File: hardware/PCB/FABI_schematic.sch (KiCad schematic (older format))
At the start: 46 parts, among them J1 Cliff_68125, J10 Conn_01x03_Male, J11 dispaly_connector_91601-304LF, J2 Cliff_68125, J3 Cliff_68125, J4 Cliff_68125, J5 Cliff_68125, J6 Cliff_68125, J7 Cliff_68125, J8 Cliff_68125, J9 Conn_02x05_Odd_Even, U1 MPXV7007GP, U2 ProMicro

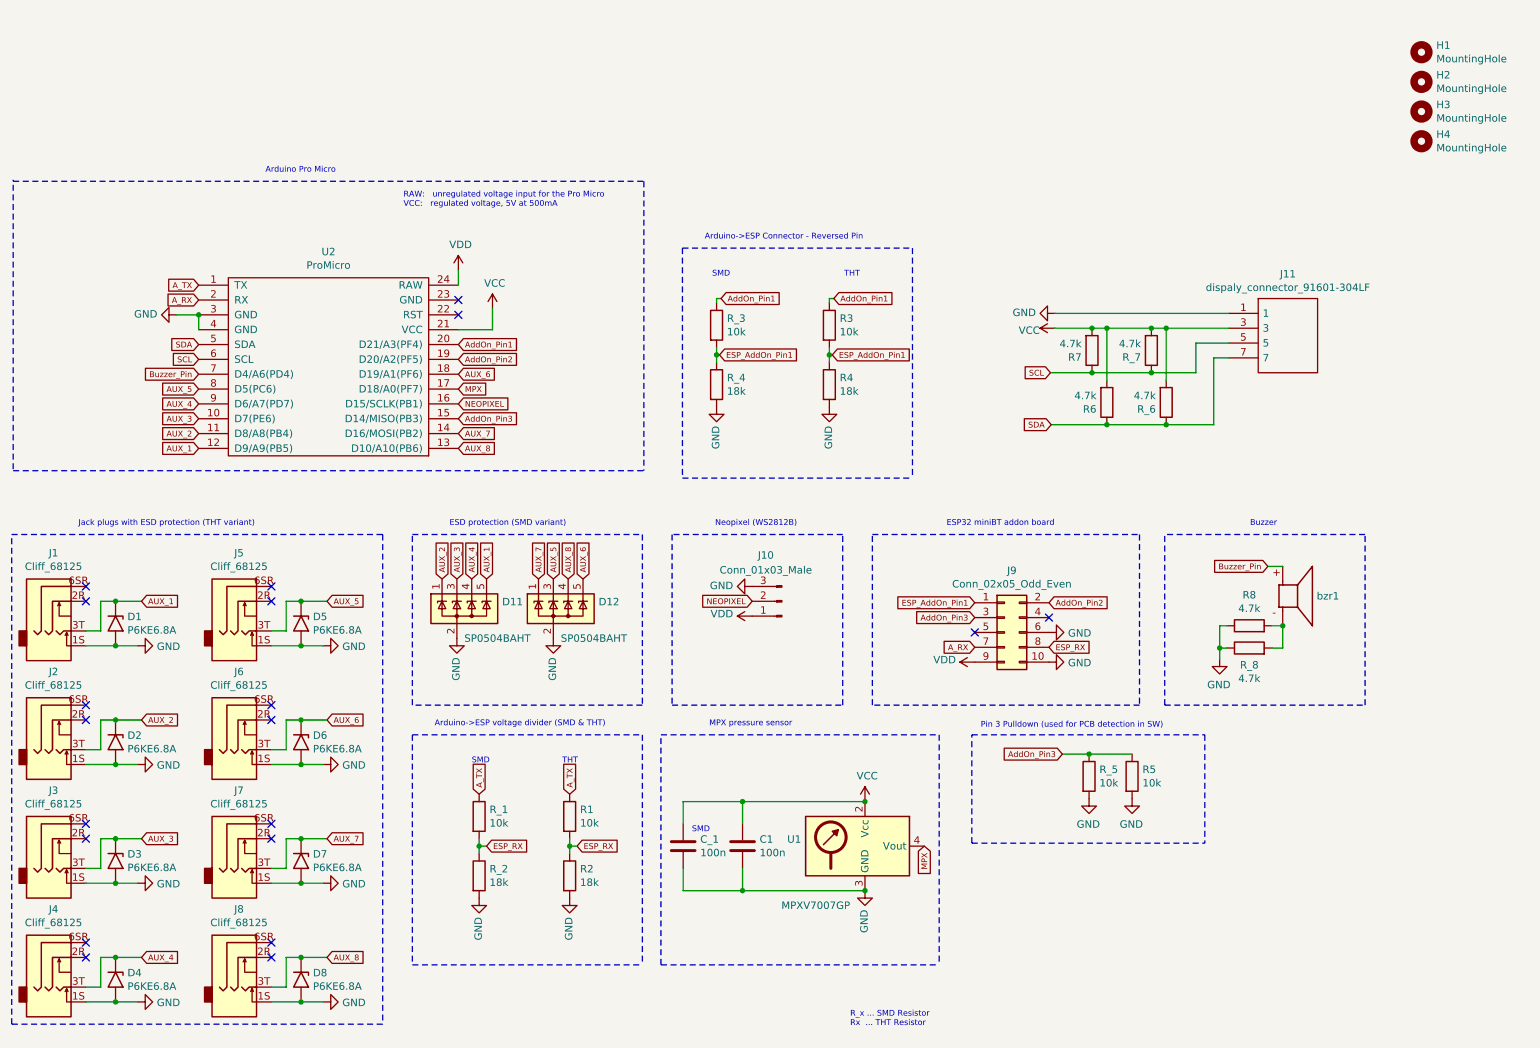
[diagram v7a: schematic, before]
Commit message: updated PCB edges, to mount PCB with M3 screws, minor changes to size and some element positions, SMD NeoPixel pads updated
Signed-off-by: fussthalerandreas <fussthaler.andreas1997@gmail.com>
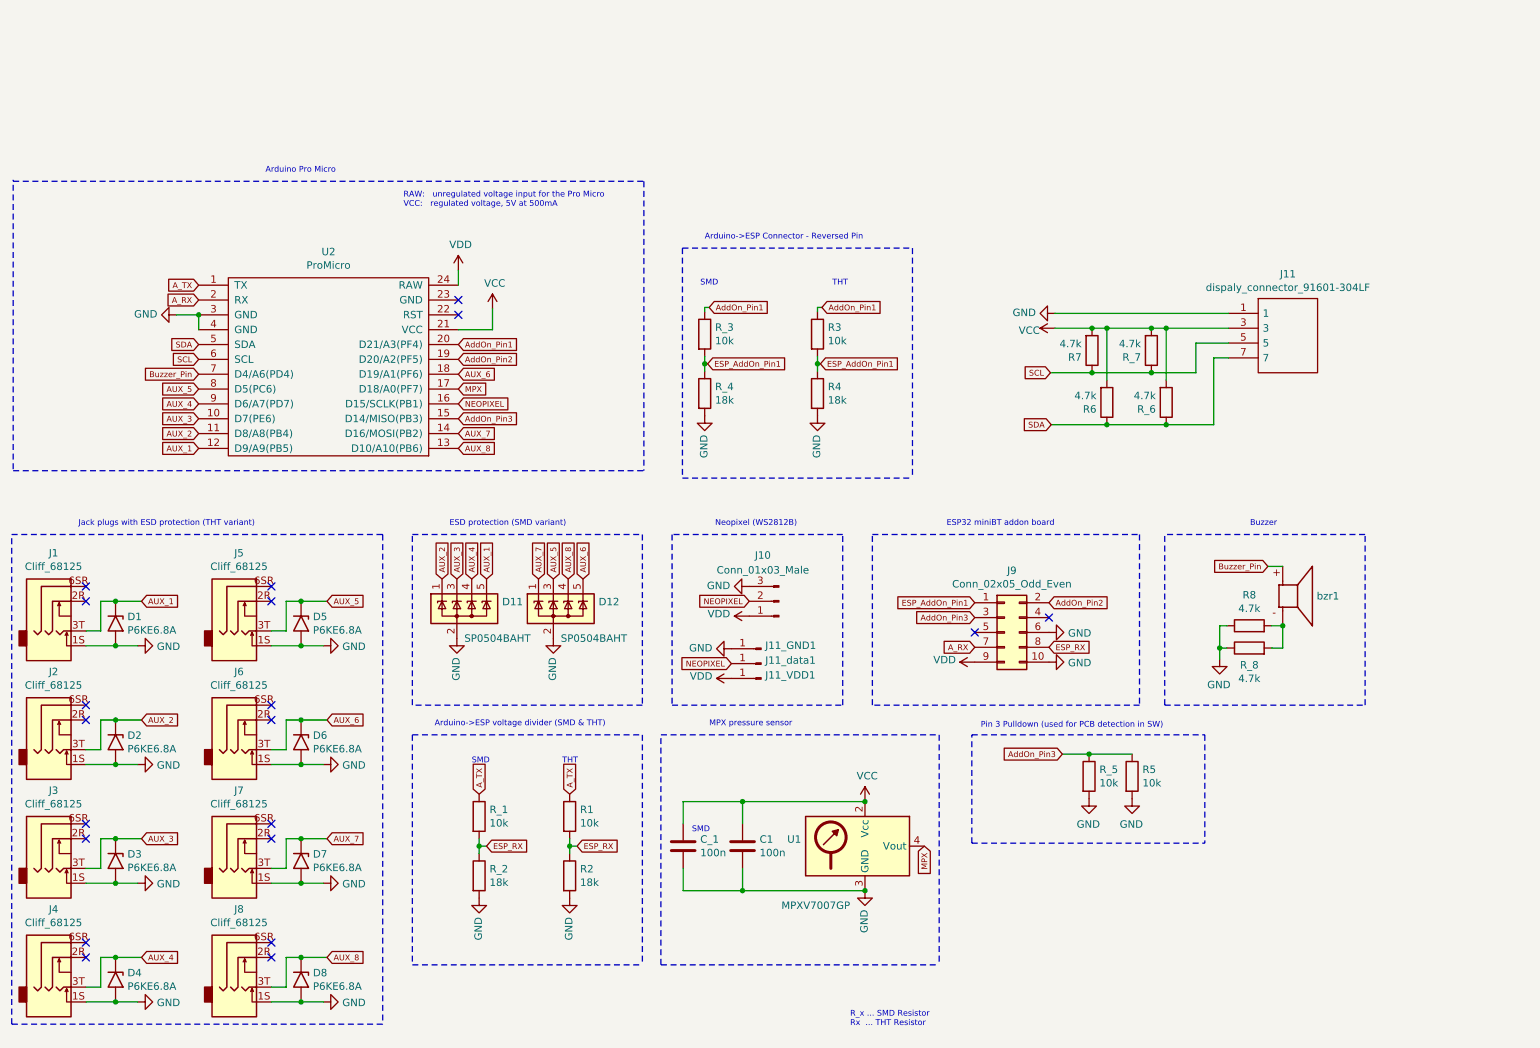
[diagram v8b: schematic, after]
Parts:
- removed H1, H2, H3, H4: MountingHole, MountingHole:MountingHole_3mm, symbol Mechanical:MountingHole
- added J11_GND1, J11_VDD1, J11_data1: Conn_01x01_Male, Connector_Wire:SolderWirePad_1x01_SMD_1x2mm, symbol Connector:Conn_01x01_Male
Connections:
- net GND: now also J11_GND1.1 (Pin_1)
- net NEOPIXEL: now also J11_data1.1 (Pin_1)
- net VDD: now also J11_VDD1.1 (Pin_1)
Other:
- moved on the sheet: J10, R3, R4, R_3, R_4
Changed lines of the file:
@@
 NoConn ~ 7590 4910
 NoConn ~ 7090 5010
-$Comp
-L Device:R R4
-U 1 1 6021AB8E
-P 6110 3340
-F 0 "R4" H 6180 3386 50  0000 L CNN
-F 1 "18k" H 6180 3295 50  0000 L CNN
-F 2 "Resistor_THT:R_Axial_DIN0204_L3.6mm_D1.6mm_P7.62mm_Horizontal" V 6040 3340 50  0001 C CNN
-F 3 "~" H 6110 3340 50  0001 C CNN
-	1    6110 3340
-	1    0    0    -1
-$EndComp
-$Comp
-L Device:R R3
-U 1 1 6021AB94
-P 6110 2940
-F 0 "R3" H 6180 2986 50  0000 L CNN
-F 1 "10k" H 6180 2895 50  0000 L CNN
-F 2 "Resistor_THT:R_Axial_DIN0204_L3.6mm_D1.6mm_P7.62mm_Horizontal" V 6040 2940 50  0001 C CNN
-F 3 "~" H 6110 2940 50  0001 C CNN
-	1    6110 2940
-	1    0    0    -1
-$EndComp
-Wire Wire Line
-	6110 3090 6110 3140
-$Comp
-L power:GND #PWR022
-U 1 1 6021AB9D
-P 6110 3490
-F 0 "#PWR022" H 6110 3240 50  0001 C CNN
-F 1 "GND" V 6115 3362 50  0000 R CNN
-F 2 "" H 6110 3490 50  0001 C CNN
-F 3 "" H 6110 3490 50  0001 C CNN
-	1    6110 3490
-	-1   0    0    -1
-$EndComp
-$Comp
-L Device:R R_4
-U 1 1 6021ABA3
-P 5350 3340
-F 0 "R_4" H 5420 3386 50  0000 L CNN
-F 1 "18k" H 5420 3295 50  0000 L CNN
-F 2 "Resistor_SMD:R_0805_2012Metric_Pad1.20x1.40mm_HandSolder" V 5280 3340 50  0001 C CNN
-F 3 "~" H 5350 3340 50  0001 C CNN
-	1    5350 3340
-	1    0    0    -1
-$EndComp
-$Comp
-L Device:R R_3
-U 1 1 6021ABA9
-P 5350 2940
-F 0 "R_3" H 5420 2986 50  0000 L CNN
-F 1 "10k" H 5420 2895 50  0000 L CNN
-F 2 "Resistor_SMD:R_0805_2012Metric_Pad1.20x1.40mm_HandSolder" V 5280 2940 50  0001 C CNN
-F 3 "~" H 5350 2940 50  0001 C CNN
-	1    5350 2940
-	1    0    0    -1
-$EndComp
-Wire Wire Line
-	5350 3090 5350 3140
-$Comp
-L power:GND #PWR021
-U 1 1 6021ABB2
-P 5350 3490
-F 0 "#PWR021" H 5350 3240 50  0001 C CNN
-F 1 "GND" V 5355 3362 50  0000 R CNN
-F 2 "" H 5350 3490 50  0001 C CNN
-F 3 "" H 5350 3490 50  0001 C CNN
-	1    5350 3490
-	-1   0    0    -1
-$EndComp
-Text Notes 6210 2620 0    39   ~ 0
+Text Notes 6130 2680 0    39   ~ 0
 THT
-Text Notes 5320 2620 0    39   ~ 0
+Text Notes 5240 2680 0    39   ~ 0
 SMD
 Wire Notes Line
@@
 	6670 2420 6670 3970
 Wire Wire Line
-	5380 2760 5350 2760
-Wire Wire Line
-	5350 2760 5350 2790
-Wire Wire Line
-	6140 2760 6110 2760
-Wire Wire Line
-	6110 2760 6110 2790
-Text GLabel 5370 3140 2    39   Input ~ 0
-ESP_AddOn_Pin1
-Text GLabel 6130 3140 2    39   Input ~ 0
-ESP_AddOn_Pin1
-Wire Wire Line
-	6130 3140 6110 3140
-Connection ~ 6110 3140
-Wire Wire Line
-	6110 3140 6110 3190
-Wire Wire Line
-	5370 3140 5350 3140
-Connection ~ 5350 3140
-Wire Wire Line
-	5350 3140 5350 3190
+	5300 2820 5270 2820
+Wire Wire Line
+	5270 2820 5270 2850
+Wire Wire Line
+	6060 2820 6030 2820
+Wire Wire Line
+	6030 2820 6030 2850
 Wire Wire Line
 	3610 2970 3840 2970
@@
 Text GLabel 3610 3470 2    39   Input ~ 0
 NEOPIXEL
-Text GLabel 5590 4800 0    39   Input ~ 0
+Text GLabel 5570 4800 0    39   Input ~ 0
 NEOPIXEL
 $Comp
 L power:GND #PWR016
 U 1 1 5F4DD6BE
-P 5590 4700
-F 0 "#PWR016" H 5590 4450 50  0001 C CNN
-F 1 "GND" V 5595 4572 50  0000 R CNN
-F 2 "" H 5590 4700 50  0001 C CNN
-F 3 "" H 5590 4700 50  0001 C CNN
-	1    5590 4700
+P 5570 4700
+F 0 "#PWR016" H 5570 4450 50  0001 C CNN
+F 1 "GND" V 5575 4572 50  0000 R CNN
+F 2 "" H 5570 4700 50  0001 C CNN
+F 3 "" H 5570 4700 50  0001 C CNN
+	1    5570 4700
 	0    1    -1   0
 $EndComp
@@
 L Connector:Conn_01x03_Male J10
 U 1 1 5F4DCE7D
-P 5790 4800
-F 0 "J10" H 5898 4490 50  0000 C CNN
-F 1 "Conn_01x03_Male" H 5898 4590 50  0000 C CNN
-F 2 "Connector_PinHeader_2.54mm:PinHeader_1x03_P2.54mm_Vertical" H 5790 4800 50  0001 C CNN
-F 3 "~" H 5790 4800 50  0001 C CNN
-	1    5790 4800
+P 5770 4800
+F 0 "J10" H 5878 4490 50  0000 C CNN
+F 1 "Conn_01x03_Male" H 5878 4590 50  0000 C CNN
+F 2 "Connector_PinHeader_2.54mm:PinHeader_1x03_P2.54mm_Vertical" H 5770 4800 50  0001 C CNN
+F 3 "~" H 5770 4800 50  0001 C CNN
+	1    5770 4800
 	-1   0    0    1
 $EndComp
@@
 L power:VDD #PWR0103
 U 1 1 6031B043
-P 5590 4900
-F 0 "#PWR0103" H 5590 4750 50  0001 C CNN
-F 1 "VDD" V 5605 5028 50  0000 L CNN
-F 2 "" H 5590 4900 50  0001 C CNN
-F 3 "" H 5590 4900 50  0001 C CNN
-	1    5590 4900
+P 5570 4900
+F 0 "#PWR0103" H 5570 4750 50  0001 C CNN
+F 1 "VDD" V 5585 5028 50  0000 L CNN
+F 2 "" H 5570 4900 50  0001 C CNN
+F 3 "" H 5570 4900 50  0001 C CNN
+	1    5570 4900
 	0    -1   -1   0
 $EndComp
 Wire Wire Line
 	8380 2960 8800 2960
-Text GLabel 6140 2760 2    39   Input ~ 0
+Text GLabel 6060 2820 2    39   Input ~ 0
 AddOn_Pin1
-Text GLabel 5380 2760 2    39   Input ~ 0
+Text GLabel 5300 2820 2    39   Input ~ 0
 AddOn_Pin1
 Text GLabel 3610 3570 2    39   Input ~ 0
@@
 Text GLabel 3610 3770 2    39   Input ~ 0
 AUX_8
-$Comp
-L Mechanical:MountingHole H1
-U 1 1 606D8EE1
-P 10100 1100
-F 0 "H1" H 10200 1146 50  0000 L CNN
-F 1 "MountingHole" H 10200 1055 50  0000 L CNN
-F 2 "MountingHole:MountingHole_3mm" H 10100 1100 50  0001 C CNN
-F 3 "~" H 10100 1100 50  0001 C CNN
-	1    10100 1100
-	1    0    0    -1
-$EndComp
-$Comp
-L Mechanical:MountingHole H2
-U 1 1 606D952C
-P 10100 1300
-F 0 "H2" H 10200 1346 50  0000 L CNN
-F 1 "MountingHole" H 10200 1255 50  0000 L CNN
-F 2 "MountingHole:MountingHole_3mm" H 10100 1300 50  0001 C CNN
-F 3 "~" H 10100 1300 50  0001 C CNN
-	1    10100 1300
-	1    0    0    -1
-$EndComp
-$Comp
-L Mechanical:MountingHole H3
-U 1 1 606DCA97
-P 10100 1500
-F 0 "H3" H 10200 1546 50  0000 L CNN
-F 1 "MountingHole" H 10200 1455 50  0000 L CNN
-F 2 "MountingHole:MountingHole_3mm" H 10100 1500 50  0001 C CNN
-F 3 "~" H 10100 1500 50  0001 C CNN
-	1    10100 1500
-	1    0    0    -1
-$EndComp
-$Comp
-L Mechanical:MountingHole H4
-U 1 1 606DFEF8
-P 10100 1700
-F 0 "H4" H 10200 1746 50  0000 L CNN
-F 1 "MountingHole" H 10200 1655 50  0000 L CNN
-F 2 "MountingHole:MountingHole_3mm" H 10100 1700 50  0001 C CNN
-F 3 "~" H 10100 1700 50  0001 C CNN
-	1    10100 1700
-	1    0    0    -1
-$EndComp
 Wire Notes Line
 	4975 5700 6850 5700
@@
 	1    0    0    1
 $EndComp
+Text GLabel 5450 5220 0    39   Input ~ 0
+NEOPIXEL
+$Comp
+L power:GND #PWR015
+U 1 1 60329107
+P 5450 5120
+F 0 "#PWR015" H 5450 4870 50  0001 C CNN
+F 1 "GND" V 5455 4992 50  0000 R CNN
+F 2 "" H 5450 5120 50  0001 C CNN
+F 3 "" H 5450 5120 50  0001 C CNN
+	1    5450 5120
+	0    1    -1   0
+$EndComp
+$Comp
+L power:VDD #PWR028
+U 1 1 6032910D
+P 5450 5320
+F 0 "#PWR028" H 5450 5170 50  0001 C CNN
+F 1 "VDD" V 5465 5448 50  0000 L CNN
+F 2 "" H 5450 5320 50  0001 C CNN
+F 3 "" H 5450 5320 50  0001 C CNN
+	1    5450 5320
+	0    -1   -1   0
+$EndComp
+$Comp
+L Connector:Conn_01x01_Male J11_data1
+U 1 1 6032D010
+P 5650 5220
+F 0 "J11_data1" H 5622 5198 50  0000 R CNN
+F 1 "Conn_01x01_Male" H 5622 5243 50  0001 R CNN
+F 2 "Connector_Wire:SolderWirePad_1x01_SMD_1x2mm" H 5650 5220 50  0001 C CNN
+F 3 "~" H 5650 5220 50  0001 C CNN
+	1    5650 5220
+	-1   0    0    1
+$EndComp
+$Comp
+L Connector:Conn_01x01_Male J11_GND1
+U 1 1 60327A50
+P 5650 5120
+F 0 "J11_GND1" H 5622 5098 50  0000 R CNN
+F 1 "Conn_01x01_Male" H 5622 5143 50  0001 R CNN
+F 2 "Connector_Wire:SolderWirePad_1x01_SMD_1x2mm" H 5650 5120 50  0001 C CNN
+F 3 "~" H 5650 5120 50  0001 C CNN
+	1    5650 5120
+	-1   0    0    1
+$EndComp
+$Comp
+L Connector:Conn_01x01_Male J11_VDD1
+U 1 1 603306CD
+P 5650 5320
+F 0 "J11_VDD1" H 5622 5298 50  0000 R CNN
+F 1 "Conn_01x01_Male" H 5622 5343 50  0001 R CNN
+F 2 "Connector_Wire:SolderWirePad_1x01_SMD_1x2mm" H 5650 5320 50  0001 C CNN
+F 3 "~" H 5650 5320 50  0001 C CNN
+	1    5650 5320
+	-1   0    0    1
+$EndComp
+Wire Wire Line
+	5270 3200 5270 3250
+Connection ~ 5270 3200
+Wire Wire Line
+	5290 3200 5270 3200
+Wire Wire Line
+	6030 3200 6030 3250
+Connection ~ 6030 3200
+Wire Wire Line
+	6050 3200 6030 3200
+Text GLabel 6050 3200 2    39   Input ~ 0
+ESP_AddOn_Pin1
+Text GLabel 5290 3200 2    39   Input ~ 0
+ESP_AddOn_Pin1
+$Comp
+L power:GND #PWR021
+U 1 1 6021ABB2
+P 5270 3550
+F 0 "#PWR021" H 5270 3300 50  0001 C CNN
+F 1 "GND" V 5275 3422 50  0000 R CNN
+F 2 "" H 5270 3550 50  0001 C CNN
+F 3 "" H 5270 3550 50  0001 C CNN
+	1    5270 3550
+	-1   0    0    -1
+$EndComp
+Wire Wire Line
+	5270 3150 5270 3200
+$Comp
+L Device:R R_3
+U 1 1 6021ABA9
+P 5270 3000
+F 0 "R_3" H 5340 3046 50  0000 L CNN
+F 1 "10k" H 5340 2955 50  0000 L CNN
+F 2 "Resistor_SMD:R_0805_2012Metric_Pad1.20x1.40mm_HandSolder" V 5200 3000 50  0001 C CNN
+F 3 "~" H 5270 3000 50  0001 C CNN
+	1    5270 3000
+	1    0    0    -1
+$EndComp
+$Comp
+L Device:R R_4
+U 1 1 6021ABA3
+P 5270 3400
+F 0 "R_4" H 5340 3446 50  0000 L CNN
+F 1 "18k" H 5340 3355 50  0000 L CNN
+F 2 "Resistor_SMD:R_0805_2012Metric_Pad1.20x1.40mm_HandSolder" V 5200 3400 50  0001 C CNN
+F 3 "~" H 5270 3400 50  0001 C CNN
+	1    5270 3400
+	1    0    0    -1
+$EndComp
+$Comp
+L power:GND #PWR022
+U 1 1 6021AB9D
+P 6030 3550
+F 0 "#PWR022" H 6030 3300 50  0001 C CNN
+F 1 "GND" V 6035 3422 50  0000 R CNN
+F 2 "" H 6030 3550 50  0001 C CNN
+F 3 "" H 6030 3550 50  0001 C CNN
+	1    6030 3550
+	-1   0    0    -1
+$EndComp
+Wire Wire Line
+	6030 3150 6030 3200
+$Comp
+L Device:R R3
+U 1 1 6021AB94
+P 6030 3000
+F 0 "R3" H 6100 3046 50  0000 L CNN
+F 1 "10k" H 6100 2955 50  0000 L CNN
+F 2 "Resistor_THT:R_Axial_DIN0204_L3.6mm_D1.6mm_P7.62mm_Horizontal" V 5960 3000 50  0001 C CNN
+F 3 "~" H 6030 3000 50  0001 C CNN
+	1    6030 3000
+	1    0    0    -1
+$EndComp
+$Comp
+L Device:R R4
+U 1 1 6021AB8E
+P 6030 3400
+F 0 "R4" H 6100 3446 50  0000 L CNN
+F 1 "18k" H 6100 3355 50  0000 L CNN
+F 2 "Resistor_THT:R_Axial_DIN0204_L3.6mm_D1.6mm_P7.62mm_Horizontal" V 5960 3400 50  0001 C CNN
+F 3 "~" H 6030 3400 50  0001 C CNN
+	1    6030 3400
+	1    0    0    -1
+$EndComp
 $EndSCHEMATC
